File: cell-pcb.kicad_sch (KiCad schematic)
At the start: 46 parts, among them J1 TC2030, J10 Mounting Hole M5, J11 Mounting Hole M5, J12 Mounting Hole M5, J13 Mounting Hole M5, J14 Mounting Hole M5, J2 Mounting Hole M5, J28 Pin Header 0.1" 01x04, J3 Mounting Hole M5, J31 172-015-243R021, J4 Mounting Hole M5, J5 Mounting Hole M5, J6 Mounting Hole M5, J7 Mounting Hole M5, J8 Mounting Hole M5, J9 Mounting Hole M5, U5 STM32F103R8T6, Y1 8MHz 20pF

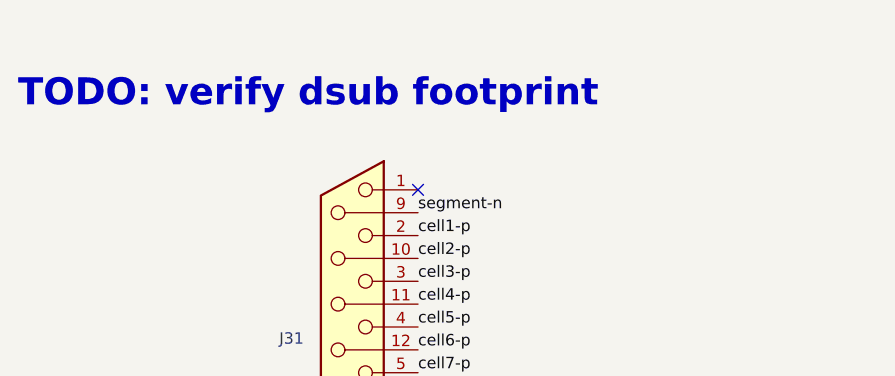
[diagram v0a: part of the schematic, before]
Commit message: fix drc/erc errors
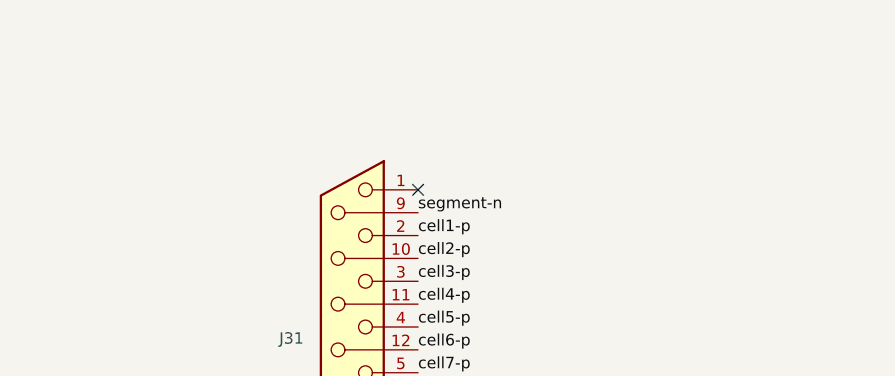
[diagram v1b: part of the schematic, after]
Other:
- note removed: "TODO: verify dsub footprint"
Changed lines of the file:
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@@
     (effects (font (size 1.27 1.27)) (justify left bottom))
-  )
-  (text "TODO: verify dsub footprint\n" (at -5.08 25.4 0)
-    (effects (font (size 3 3) (thickness 0.8) bold (color 255 4 17 1)) (justify left bottom))
   )
   (text "Programming/debug header.\nPlace in an accessible location close to the mcu."

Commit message: Created test firmware
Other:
- note added: "Kamaya HFC32202AGTP"
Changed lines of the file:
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@@
     (effects (font (size 2.0066 2.0066) (thickness 0.4013) bold) (justify left bottom))
+  )
+  (text "Kamaya HFC32202AGTP" (at 120.65 77.47 0)
+    (effects (font (size 1.27 1.27)) (justify left bottom))
   )
   (text "1x bulk decoupling + 100nF per VDD pin" (at 95.25 149.86 0)

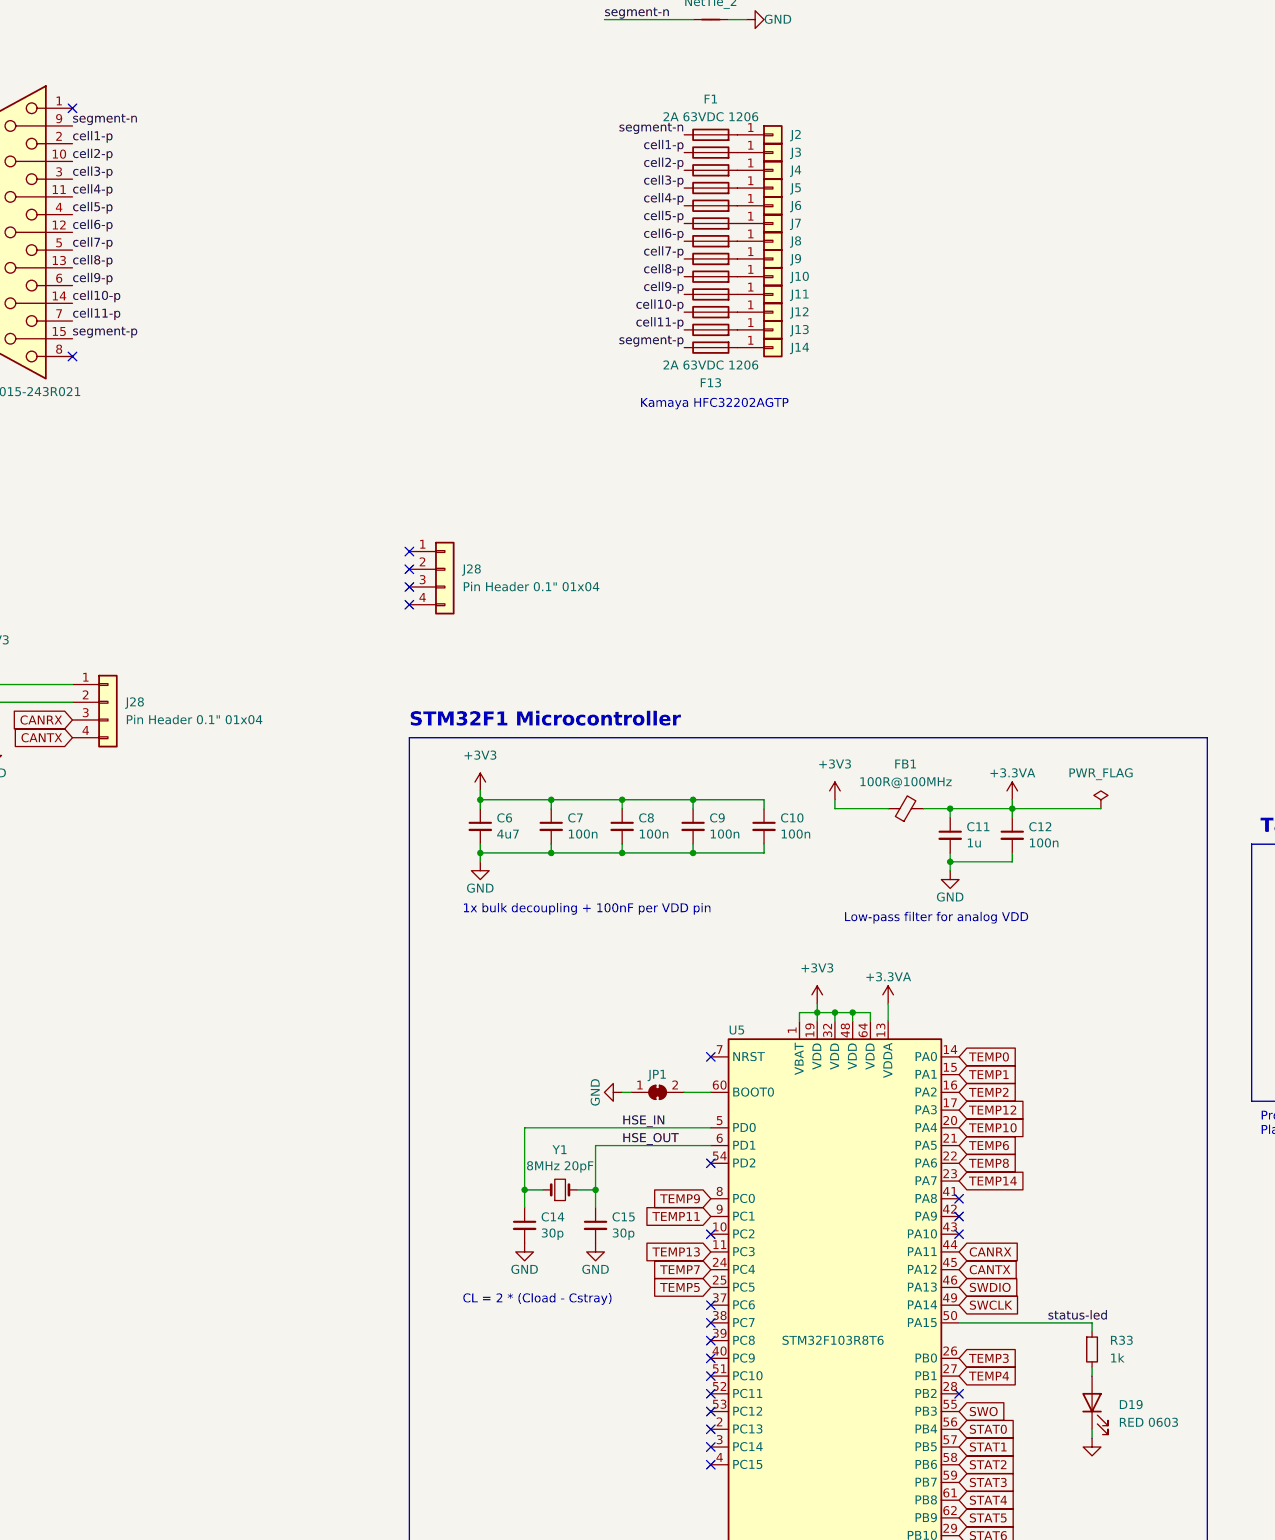
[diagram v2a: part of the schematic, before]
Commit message: update firmware to do calibration and work with orion BMS
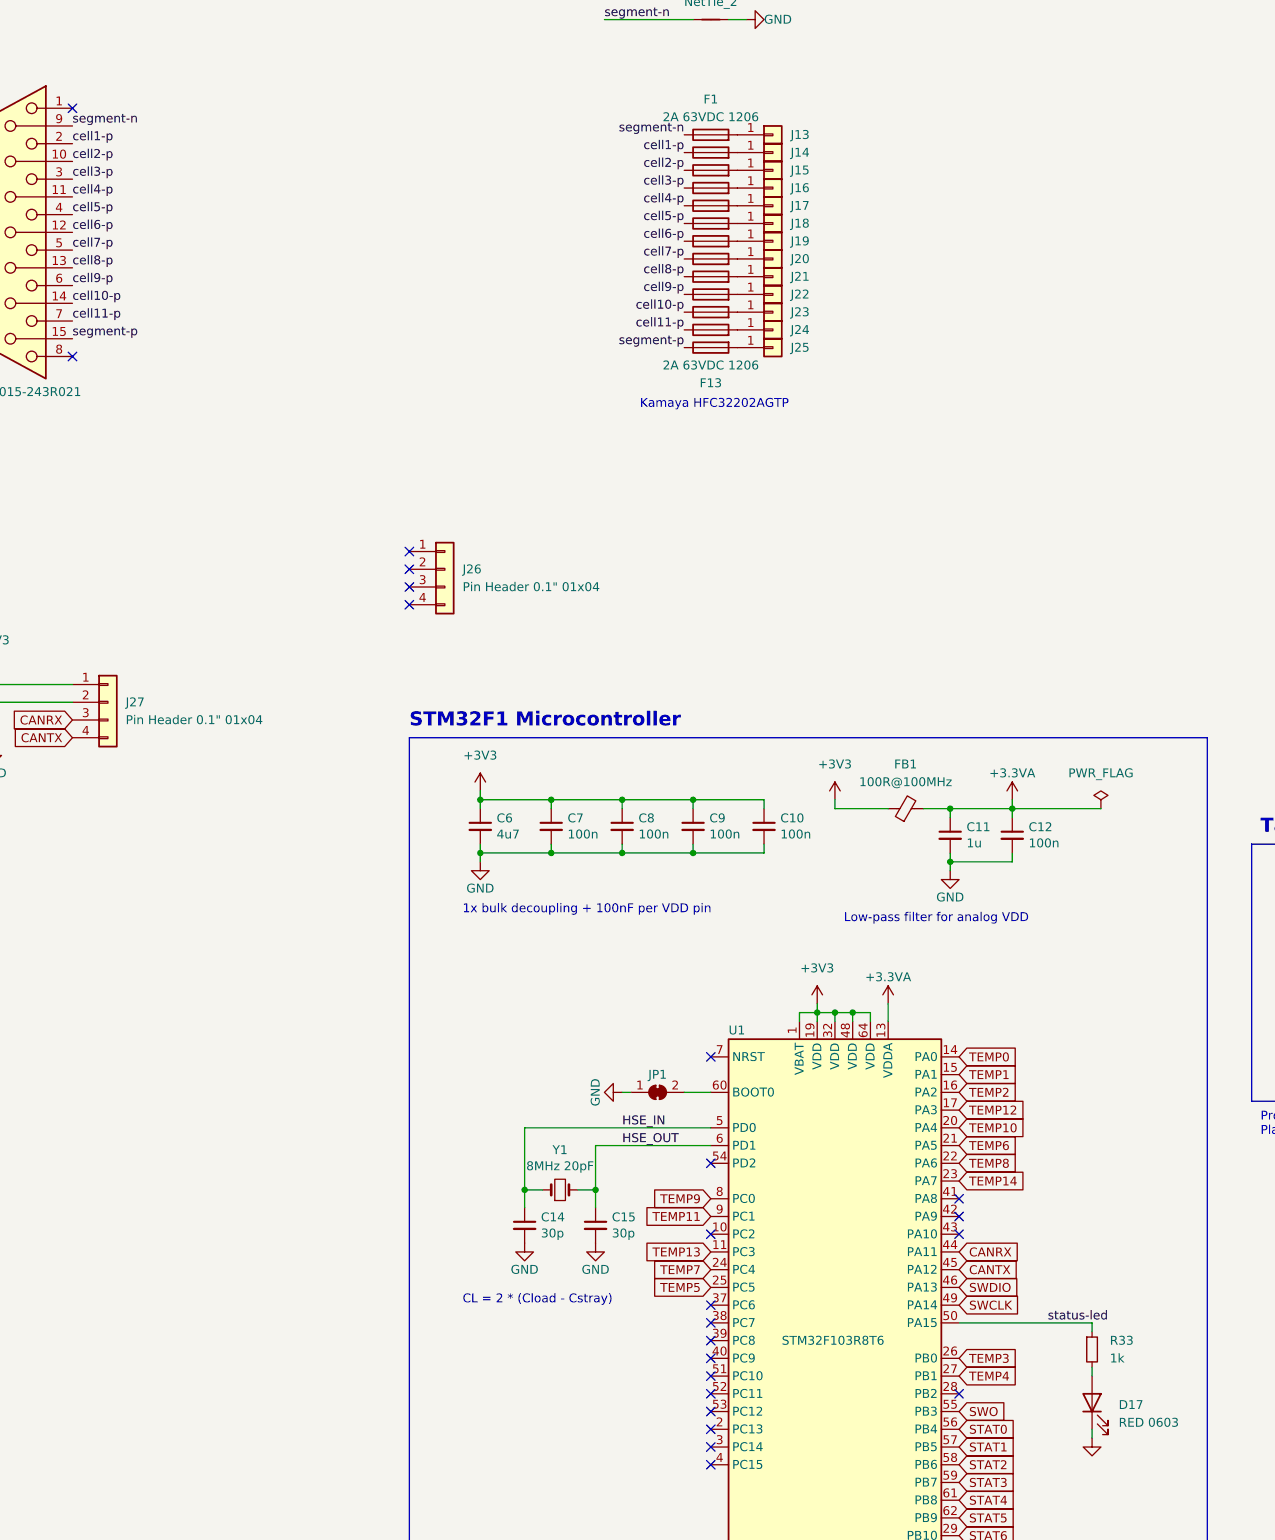
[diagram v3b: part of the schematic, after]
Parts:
- renumbered D19 to D17, J2 to J13, J3 to J14, J4 to J15, J5 to J16, J6 to J17, J7 to J18, J8 to J19, J9 to J20, J10 to J21, J11 to J22, J12 to J23, J13 to J24, J14 to J25, J28 to J26, J28 to J27, U5 to U1

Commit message: Kicad Update
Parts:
- renumbered C6 to C17, C7 to C18, C8 to C19, C9 to C20, C10 to C21, C11 to C22, C12 to C23, C14 to C24, C15 to C25, J1 to J28
